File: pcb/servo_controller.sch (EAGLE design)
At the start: 54 parts, among them IC1 PIC18F452, IC2 LM2936MP-3.0, Q1 10Mhz, U1 ARDUINOR3-DIMENSION

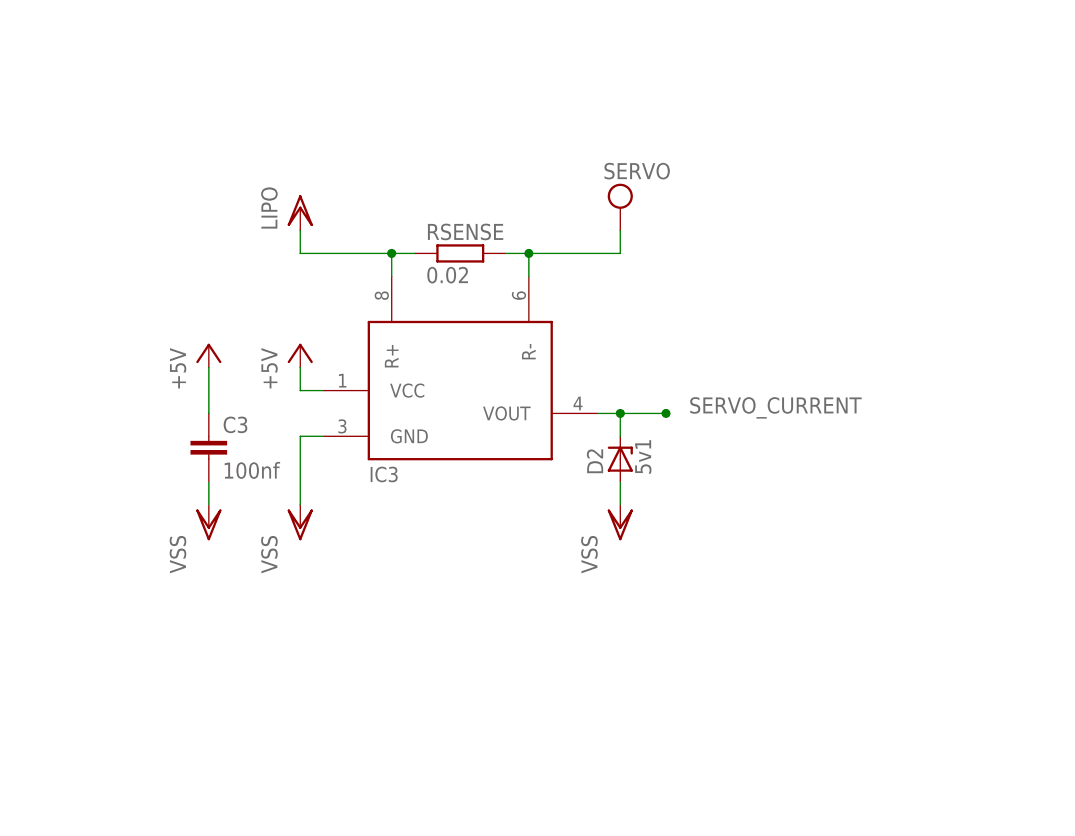
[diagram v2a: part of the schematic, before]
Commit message: Added sot23 footprint for max4173
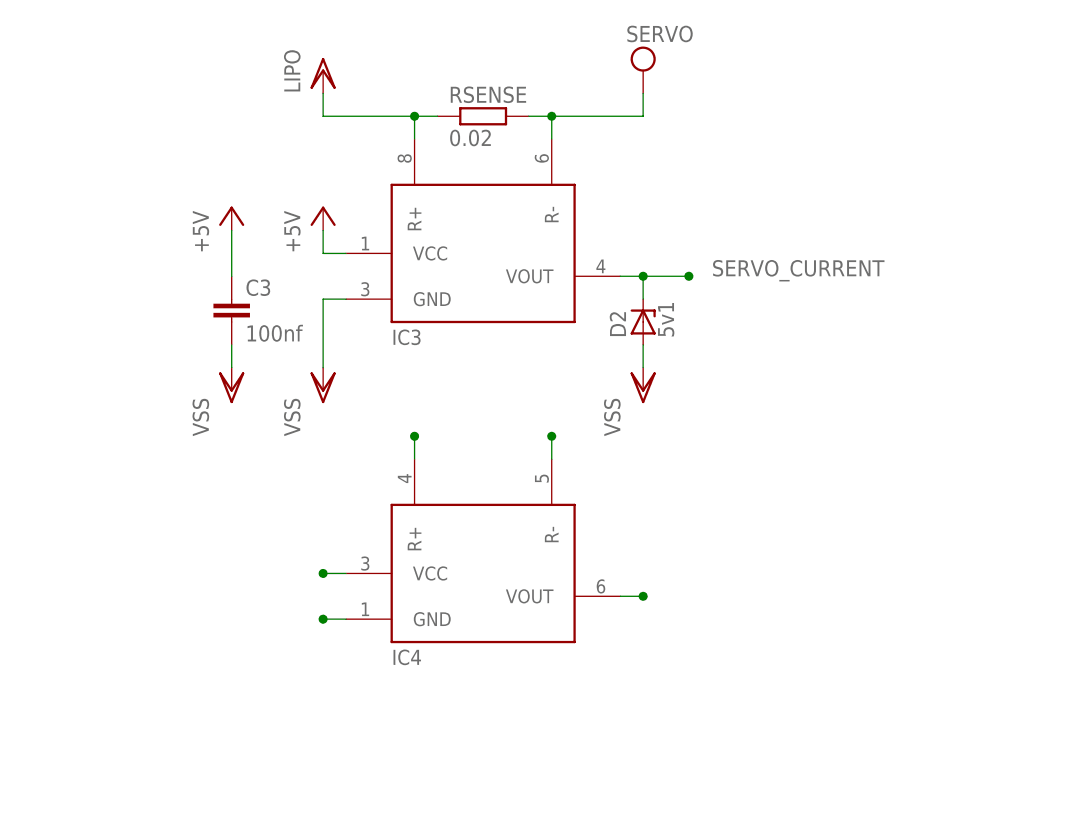
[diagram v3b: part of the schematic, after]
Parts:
- added IC4: (no value), AWJLEagleLib:MAX4173T
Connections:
- net +5V: now also IC4.VCC
- net SERVO_CURRENT: now also IC4.VOUT
- net VDD: now also IC4.R+
- net VEE: now also IC4.R-
- net VSS: now also IC4.GND
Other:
- moved on the sheet: C3, D2, IC3, RSENSE
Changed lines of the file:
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@@
 <part name="VSS27" library="supply1" deviceset="VSS" device=""/>
 <part name="PW" library="switch" deviceset="TL36PO" device=""/>
+<part name="IC4" library="AWJLEagleLib" deviceset="MAX4173" device="T"/>
 </parts>
 <sheets>
@@
 <instance part="VSS6" gate="G$1" x="48.26" y="177.8"/>
 <instance part="P+1" gate="1" x="121.92" y="215.9"/>
-<instance part="P+8" gate="1" x="193.04" y="200.66"/>
+<instance part="P+8" gate="1" x="195.58" y="215.9"/>
 <instance part="VSS7" gate="G$1" x="109.22" y="177.8"/>
 <instance part="VDD1" gate="G$1" x="48.26" y="215.9"/>
@@
 <instance part="SUPPLY3" gate="G$1" x="81.28" y="30.48"/>
 <instance part="SUPPLY4" gate="G$1" x="147.32" y="40.64"/>
-<instance part="IC3" gate="G$1" x="210.82" y="195.58"/>
-<instance part="VSS14" gate="G$1" x="193.04" y="180.34"/>
-<instance part="VDD2" gate="G$1" x="193.04" y="215.9"/>
+<instance part="IC3" gate="G$1" x="213.36" y="210.82"/>
+<instance part="VSS14" gate="G$1" x="195.58" y="195.58"/>
+<instance part="VDD2" gate="G$1" x="195.58" y="231.14"/>
 <instance part="RESET" gate="G$1" x="114.3" y="129.54" smashed="yes">
 <attribute name="NAME" x="114.935" y="130.81" size="1.778" layer="95" rot="R90"/>
@@
 <attribute name="TP_SIGNAL_NAME" x="125.73" y="128.27" size="1.778" layer="97"/>
 </instance>
-<instance part="SUPPLY5" gate="G$1" x="228.6" y="215.9"/>
+<instance part="SUPPLY5" gate="G$1" x="231.14" y="231.14"/>
 <instance part="VSS16" gate="G$1" x="134.62" y="101.6"/>
 <instance part="VSS17" gate="G$1" x="53.34" y="20.32"/>
@@
 </instance>
 <instance part="D1" gate="G$1" x="114.3" y="210.82"/>
-<instance part="C3" gate="G$1" x="182.88" y="190.5"/>
-<instance part="P+6" gate="1" x="182.88" y="200.66"/>
-<instance part="VSS8" gate="G$1" x="182.88" y="180.34"/>
+<instance part="C3" gate="G$1" x="185.42" y="205.74"/>
+<instance part="P+6" gate="1" x="185.42" y="215.9"/>
+<instance part="VSS8" gate="G$1" x="185.42" y="195.58"/>
 <instance part="EXT" gate="1" x="299.72" y="50.8"/>
 <instance part="C5" gate="G$1" x="60.96" y="30.48"/>
 <instance part="VSS22" gate="G$1" x="60.96" y="20.32"/>
-<instance part="RSENSE" gate="G$1" x="210.82" y="210.82"/>
+<instance part="RSENSE" gate="G$1" x="213.36" y="226.06"/>
 <instance part="C4" gate="G$1" x="182.88" y="27.94"/>
 <instance part="VSS23" gate="G$1" x="182.88" y="17.78"/>
@@
 <instance part="R7" gate="G$1" x="83.82" y="93.98" rot="R90"/>
 <instance part="P+9" gate="1" x="83.82" y="104.14"/>
-<instance part="D2" gate="G$1" x="228.6" y="187.96" rot="R90"/>
+<instance part="D2" gate="G$1" x="231.14" y="203.2" rot="R90"/>
 <instance part="D3" gate="G$1" x="55.88" y="187.96" rot="R90"/>
 <instance part="VSS25" gate="G$1" x="55.88" y="177.8"/>
-<instance part="VSS26" gate="G$1" x="228.6" y="180.34"/>
+<instance part="VSS26" gate="G$1" x="231.14" y="195.58"/>
 <instance part="SJ1" gate="1" x="332.74" y="129.54" rot="R90"/>
 <instance part="C9" gate="G$1" x="119.38" y="198.12"/>
 <instance part="VSS27" gate="G$1" x="119.38" y="177.8"/>
 <instance part="PW" gate="BEF1" x="35.56" y="208.28" rot="R270"/>
+<instance part="IC4" gate="G$1" x="213.36" y="175.26"/>
 </instances>
 <busses>
@@
 <segment>
 <pinref part="IC3" gate="G$1" pin="GND"/>
-<wire x1="195.58" y1="190.5" x2="193.04" y2="190.5" width="0.1524" layer="91"/>
+<wire x1="198.12" y1="205.74" x2="195.58" y2="205.74" width="0.1524" layer="91"/>
 <pinref part="VSS14" gate="G$1" pin="VSS"/>
-<wire x1="193.04" y1="190.5" x2="193.04" y2="182.88" width="0.1524" layer="91"/>
+<wire x1="195.58" y1="205.74" x2="195.58" y2="198.12" width="0.1524" layer="91"/>
 </segment>
 <segment>
@@
 <pinref part="C3" gate="G$1" pin="2"/>
 <pinref part="VSS8" gate="G$1" pin="VSS"/>
-<wire x1="182.88" y1="182.88" x2="182.88" y2="185.42" width="0.1524" layer="91"/>
+<wire x1="185.42" y1="198.12" x2="185.42" y2="200.66" width="0.1524" layer="91"/>
 </segment>
 <segment>
@@
 <pinref part="D2" gate="G$1" pin="A"/>
 <pinref part="VSS26" gate="G$1" pin="VSS"/>
-<wire x1="228.6" y1="182.88" x2="228.6" y2="185.42" width="0.1524" layer="91"/>
+<wire x1="231.14" y1="198.12" x2="231.14" y2="200.66" width="0.1524" layer="91"/>
 </segment>
 <segment>
@@
 <pinref part="VSS27" gate="G$1" pin="VSS"/>
 <wire x1="119.38" y1="180.34" x2="119.38" y2="193.04" width="0.1524" layer="91"/>
+</segment>
+<segment>
+<pinref part="IC4" gate="G$1" pin="GND"/>
+<wire x1="198.12" y1="170.18" x2="195.58" y2="170.18" width="0.1524" layer="91"/>
+<junction x="195.58" y="170.18"/>
 </segment>
 </net>
@@
 <segment>
 <pinref part="IC3" gate="G$1" pin="VCC"/>
-<wire x1="195.58" y1="195.58" x2="193.04" y2="195.58" width="0.1524" layer="91"/>
+<wire x1="198.12" y1="210.82" x2="195.58" y2="210.82" width="0.1524" layer="91"/>
 <pinref part="P+8" gate="1" pin="+5V"/>
-<wire x1="193.04" y1="195.58" x2="193.04" y2="198.12" width="0.1524" layer="91"/>
+<wire x1="195.58" y1="210.82" x2="195.58" y2="213.36" width="0.1524" layer="91"/>
 </segment>
 <segment>
 <pinref part="P+6" gate="1" pin="+5V"/>
 <pinref part="C3" gate="G$1" pin="1"/>
-<wire x1="182.88" y1="193.04" x2="182.88" y2="198.12" width="0.1524" layer="91"/>
+<wire x1="185.42" y1="208.28" x2="185.42" y2="213.36" width="0.1524" layer="91"/>
 </segment>
 <segment>
@@
 <pinref part="P+9" gate="1" pin="+5V"/>
 <wire x1="83.82" y1="101.6" x2="83.82" y2="99.06" width="0.1524" layer="91"/>
+</segment>
+<segment>
+<pinref part="IC4" gate="G$1" pin="VCC"/>
+<wire x1="198.12" y1="175.26" x2="195.58" y2="175.26" width="0.1524" layer="91"/>
+<junction x="195.58" y="175.26"/>
 </segment>
 </net>
@@
 <segment>
 <pinref part="VDD2" gate="G$1" pin="VDD"/>
-<wire x1="193.04" y1="213.36" x2="193.04" y2="210.82" width="0.1524" layer="91"/>
-<wire x1="193.04" y1="210.82" x2="203.2" y2="210.82" width="0.1524" layer="91"/>
+<wire x1="195.58" y1="228.6" x2="195.58" y2="226.06" width="0.1524" layer="91"/>
+<wire x1="195.58" y1="226.06" x2="205.74" y2="226.06" width="0.1524" layer="91"/>
 <pinref part="IC3" gate="G$1" pin="R+"/>
-<wire x1="203.2" y1="210.82" x2="203.2" y2="208.28" width="0.1524" layer="91"/>
-<wire x1="203.2" y1="210.82" x2="205.74" y2="210.82" width="0.1524" layer="91"/>
-<junction x="203.2" y="210.82"/>
+<wire x1="205.74" y1="226.06" x2="205.74" y2="223.52" width="0.1524" layer="91"/>
+<wire x1="205.74" y1="226.06" x2="208.28" y2="226.06" width="0.1524" layer="91"/>
+<junction x="205.74" y="226.06"/>
 <pinref part="RSENSE" gate="G$1" pin="1"/>
+</segment>
+<segment>
+<pinref part="IC4" gate="G$1" pin="R+"/>
+<wire x1="205.74" y1="187.96" x2="205.74" y2="190.5" width="0.1524" layer="91"/>
+<junction x="205.74" y="190.5"/>
 </segment>
 </net>
@@
 <segment>
 <pinref part="IC3" gate="G$1" pin="R-"/>
-<wire x1="218.44" y1="208.28" x2="218.44" y2="210.82" width="0.1524" layer="91"/>
-<wire x1="218.44" y1="210.82" x2="228.6" y2="210.82" width="0.1524" layer="91"/>
+<wire x1="220.98" y1="223.52" x2="220.98" y2="226.06" width="0.1524" layer="91"/>
+<wire x1="220.98" y1="226.06" x2="231.14" y2="226.06" width="0.1524" layer="91"/>
 <pinref part="SUPPLY5" gate="G$1" pin="VEE"/>
-<wire x1="228.6" y1="210.82" x2="228.6" y2="213.36" width="0.1524" layer="91"/>
-<wire x1="215.9" y1="210.82" x2="218.44" y2="210.82" width="0.1524" layer="91"/>
-<junction x="218.44" y="210.82"/>
+<wire x1="231.14" y1="226.06" x2="231.14" y2="228.6" width="0.1524" layer="91"/>
+<wire x1="218.44" y1="226.06" x2="220.98" y2="226.06" width="0.1524" layer="91"/>
+<junction x="220.98" y="226.06"/>
 <pinref part="RSENSE" gate="G$1" pin="2"/>
 </segment>
+<segment>
+<pinref part="IC4" gate="G$1" pin="R-"/>
+<wire x1="220.98" y1="187.96" x2="220.98" y2="190.5" width="0.1524" layer="91"/>
+<junction x="220.98" y="190.5"/>
+</segment>
 </net>
 <net name="SERVO_CURRENT" class="0">
 <segment>
 <pinref part="IC3" gate="G$1" pin="VOUT"/>
-<wire x1="226.06" y1="193.04" x2="228.6" y2="193.04" width="0.1524" layer="91"/>
-<junction x="233.68" y="193.04"/>
-<label x="236.22" y="193.04" size="1.778" layer="95"/>
+<wire x1="228.6" y1="208.28" x2="231.14" y2="208.28" width="0.1524" layer="91"/>
+<junction x="236.22" y="208.28"/>
+<label x="238.76" y="208.28" size="1.778" layer="95"/>
 <pinref part="D2" gate="G$1" pin="C"/>
-<wire x1="228.6" y1="193.04" x2="233.68" y2="193.04" width="0.1524" layer="91"/>
-<wire x1="228.6" y1="193.04" x2="228.6" y2="190.5" width="0.1524" layer="91"/>
-<junction x="228.6" y="193.04"/>
+<wire x1="231.14" y1="208.28" x2="236.22" y2="208.28" width="0.1524" layer="91"/>
+<wire x1="231.14" y1="208.28" x2="231.14" y2="205.74" width="0.1524" layer="91"/>
+<junction x="231.14" y="208.28"/>
 </segment>
 <segment>
@@
 <label x="353.06" y="116.84" size="1.778" layer="95" rot="R90"/>
 </segment>
-</net>
+<segment>
+<pinref part="IC4" gate="G$1" pin="VOUT"/>
+<wire x1="228.6" y1="172.72" x2="231.14" y2="172.72" width="0.1524" layer="91"/>
+<junction x="231.14" y="172.72"/>
+</segment>
+</net>

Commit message: Misc
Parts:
- IC3: value (none) -> MAX4173FESA+
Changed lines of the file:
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@@
 <part name="SUPPLY3" library="supply2" deviceset="VEE" device="" value="SERVO"/>
 <part name="SUPPLY4" library="supply2" deviceset="VEE" device="" value="SERVO"/>
-<part name="IC3" library="AWJLEagleLib" deviceset="MAX4173" device="A"/>
+<part name="IC3" library="AWJLEagleLib" deviceset="MAX4173" device="A" value="MAX4173FESA+"/>
 <part name="VSS14" library="supply1" deviceset="VSS" device=""/>
 <part name="VDD2" library="supply1" deviceset="VDD" device="" value="LIPO"/>

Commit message: Elec
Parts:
- removed IC4: (no value), AWJLEagleLib:MAX4173T
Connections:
- net +5V: no longer IC4.VCC
- net SERVO_CURRENT: no longer IC4.VOUT
- net VDD: no longer IC4.R+
- net VEE: no longer IC4.R-
- net VSS: no longer IC4.GND
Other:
- moved on the sheet: C3, D2, IC3, RSENSE
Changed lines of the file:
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@@
 <part name="VSS27" library="supply1" deviceset="VSS" device=""/>
 <part name="PW" library="switch" deviceset="TL36PO" device=""/>
-<part name="IC4" library="AWJLEagleLib" deviceset="MAX4173" device="T"/>
 </parts>
 <sheets>
@@
 <instance part="VSS6" gate="G$1" x="48.26" y="177.8"/>
 <instance part="P+1" gate="1" x="121.92" y="215.9"/>
-<instance part="P+8" gate="1" x="195.58" y="215.9"/>
+<instance part="P+8" gate="1" x="198.12" y="205.74"/>
 <instance part="VSS7" gate="G$1" x="109.22" y="177.8"/>
 <instance part="VDD1" gate="G$1" x="48.26" y="215.9"/>
@@
 <instance part="SUPPLY3" gate="G$1" x="81.28" y="30.48"/>
 <instance part="SUPPLY4" gate="G$1" x="147.32" y="40.64"/>
-<instance part="IC3" gate="G$1" x="213.36" y="210.82"/>
-<instance part="VSS14" gate="G$1" x="195.58" y="195.58"/>
-<instance part="VDD2" gate="G$1" x="195.58" y="231.14"/>
+<instance part="IC3" gate="G$1" x="215.9" y="200.66"/>
+<instance part="VSS14" gate="G$1" x="198.12" y="185.42"/>
+<instance part="VDD2" gate="G$1" x="198.12" y="220.98"/>
 <instance part="RESET" gate="G$1" x="114.3" y="129.54" smashed="yes">
 <attribute name="NAME" x="114.935" y="130.81" size="1.778" layer="95" rot="R90"/>
@@
 <attribute name="TP_SIGNAL_NAME" x="125.73" y="128.27" size="1.778" layer="97"/>
 </instance>
-<instance part="SUPPLY5" gate="G$1" x="231.14" y="231.14"/>
+<instance part="SUPPLY5" gate="G$1" x="233.68" y="220.98"/>
 <instance part="VSS16" gate="G$1" x="134.62" y="101.6"/>
 <instance part="VSS17" gate="G$1" x="53.34" y="20.32"/>
@@
 </instance>
 <instance part="D1" gate="G$1" x="114.3" y="210.82"/>
-<instance part="C3" gate="G$1" x="185.42" y="205.74"/>
-<instance part="P+6" gate="1" x="185.42" y="215.9"/>
-<instance part="VSS8" gate="G$1" x="185.42" y="195.58"/>
+<instance part="C3" gate="G$1" x="187.96" y="195.58"/>
+<instance part="P+6" gate="1" x="187.96" y="205.74"/>
+<instance part="VSS8" gate="G$1" x="187.96" y="185.42"/>
 <instance part="EXT" gate="1" x="299.72" y="50.8"/>
 <instance part="C5" gate="G$1" x="60.96" y="30.48"/>
 <instance part="VSS22" gate="G$1" x="60.96" y="20.32"/>
-<instance part="RSENSE" gate="G$1" x="213.36" y="226.06"/>
+<instance part="RSENSE" gate="G$1" x="215.9" y="215.9"/>
 <instance part="C4" gate="G$1" x="182.88" y="27.94"/>
 <instance part="VSS23" gate="G$1" x="182.88" y="17.78"/>
@@
 <instance part="R7" gate="G$1" x="83.82" y="93.98" rot="R90"/>
 <instance part="P+9" gate="1" x="83.82" y="104.14"/>
-<instance part="D2" gate="G$1" x="231.14" y="203.2" rot="R90"/>
+<instance part="D2" gate="G$1" x="233.68" y="193.04" rot="R90"/>
 <instance part="D3" gate="G$1" x="55.88" y="187.96" rot="R90"/>
 <instance part="VSS25" gate="G$1" x="55.88" y="177.8"/>
-<instance part="VSS26" gate="G$1" x="231.14" y="195.58"/>
+<instance part="VSS26" gate="G$1" x="233.68" y="185.42"/>
 <instance part="SJ1" gate="1" x="332.74" y="129.54" rot="R90"/>
 <instance part="C9" gate="G$1" x="119.38" y="198.12"/>
 <instance part="VSS27" gate="G$1" x="119.38" y="177.8"/>
 <instance part="PW" gate="BEF1" x="35.56" y="208.28" rot="R270"/>
-<instance part="IC4" gate="G$1" x="213.36" y="175.26"/>
 </instances>
 <busses>
@@
 <segment>
 <pinref part="IC3" gate="G$1" pin="GND"/>
-<wire x1="198.12" y1="205.74" x2="195.58" y2="205.74" width="0.1524" layer="91"/>
+<wire x1="200.66" y1="195.58" x2="198.12" y2="195.58" width="0.1524" layer="91"/>
 <pinref part="VSS14" gate="G$1" pin="VSS"/>
-<wire x1="195.58" y1="205.74" x2="195.58" y2="198.12" width="0.1524" layer="91"/>
+<wire x1="198.12" y1="195.58" x2="198.12" y2="187.96" width="0.1524" layer="91"/>
 </segment>
 <segment>
@@
 <pinref part="C3" gate="G$1" pin="2"/>
 <pinref part="VSS8" gate="G$1" pin="VSS"/>
-<wire x1="185.42" y1="198.12" x2="185.42" y2="200.66" width="0.1524" layer="91"/>
+<wire x1="187.96" y1="187.96" x2="187.96" y2="190.5" width="0.1524" layer="91"/>
 </segment>
 <segment>
@@
 <pinref part="D2" gate="G$1" pin="A"/>
 <pinref part="VSS26" gate="G$1" pin="VSS"/>
-<wire x1="231.14" y1="198.12" x2="231.14" y2="200.66" width="0.1524" layer="91"/>
+<wire x1="233.68" y1="187.96" x2="233.68" y2="190.5" width="0.1524" layer="91"/>
 </segment>
 <segment>
@@
 <pinref part="VSS27" gate="G$1" pin="VSS"/>
 <wire x1="119.38" y1="180.34" x2="119.38" y2="193.04" width="0.1524" layer="91"/>
-</segment>
-<segment>
-<pinref part="IC4" gate="G$1" pin="GND"/>
-<wire x1="198.12" y1="170.18" x2="195.58" y2="170.18" width="0.1524" layer="91"/>
-<junction x="195.58" y="170.18"/>
 </segment>
 </net>
@@
 <segment>
 <pinref part="IC3" gate="G$1" pin="VCC"/>
-<wire x1="198.12" y1="210.82" x2="195.58" y2="210.82" width="0.1524" layer="91"/>
+<wire x1="200.66" y1="200.66" x2="198.12" y2="200.66" width="0.1524" layer="91"/>
 <pinref part="P+8" gate="1" pin="+5V"/>
-<wire x1="195.58" y1="210.82" x2="195.58" y2="213.36" width="0.1524" layer="91"/>
+<wire x1="198.12" y1="200.66" x2="198.12" y2="203.2" width="0.1524" layer="91"/>
 </segment>
 <segment>
 <pinref part="P+6" gate="1" pin="+5V"/>
 <pinref part="C3" gate="G$1" pin="1"/>
-<wire x1="185.42" y1="208.28" x2="185.42" y2="213.36" width="0.1524" layer="91"/>
+<wire x1="187.96" y1="198.12" x2="187.96" y2="203.2" width="0.1524" layer="91"/>
 </segment>
 <segment>
@@
 <pinref part="P+9" gate="1" pin="+5V"/>
 <wire x1="83.82" y1="101.6" x2="83.82" y2="99.06" width="0.1524" layer="91"/>
-</segment>
-<segment>
-<pinref part="IC4" gate="G$1" pin="VCC"/>
-<wire x1="198.12" y1="175.26" x2="195.58" y2="175.26" width="0.1524" layer="91"/>
-<junction x="195.58" y="175.26"/>
 </segment>
 </net>
@@
 <segment>
 <pinref part="VDD2" gate="G$1" pin="VDD"/>
-<wire x1="195.58" y1="228.6" x2="195.58" y2="226.06" width="0.1524" layer="91"/>
-<wire x1="195.58" y1="226.06" x2="205.74" y2="226.06" width="0.1524" layer="91"/>
+<wire x1="198.12" y1="218.44" x2="198.12" y2="215.9" width="0.1524" layer="91"/>
+<wire x1="198.12" y1="215.9" x2="208.28" y2="215.9" width="0.1524" layer="91"/>
 <pinref part="IC3" gate="G$1" pin="R+"/>
-<wire x1="205.74" y1="226.06" x2="205.74" y2="223.52" width="0.1524" layer="91"/>
-<wire x1="205.74" y1="226.06" x2="208.28" y2="226.06" width="0.1524" layer="91"/>
-<junction x="205.74" y="226.06"/>
+<wire x1="208.28" y1="215.9" x2="208.28" y2="213.36" width="0.1524" layer="91"/>
+<wire x1="208.28" y1="215.9" x2="210.82" y2="215.9" width="0.1524" layer="91"/>
+<junction x="208.28" y="215.9"/>
 <pinref part="RSENSE" gate="G$1" pin="1"/>
-</segment>
-<segment>
-<pinref part="IC4" gate="G$1" pin="R+"/>
-<wire x1="205.74" y1="187.96" x2="205.74" y2="190.5" width="0.1524" layer="91"/>
-<junction x="205.74" y="190.5"/>
 </segment>
 </net>
@@
 <segment>
 <pinref part="IC3" gate="G$1" pin="R-"/>
-<wire x1="220.98" y1="223.52" x2="220.98" y2="226.06" width="0.1524" layer="91"/>
-<wire x1="220.98" y1="226.06" x2="231.14" y2="226.06" width="0.1524" layer="91"/>
+<wire x1="223.52" y1="213.36" x2="223.52" y2="215.9" width="0.1524" layer="91"/>
+<wire x1="223.52" y1="215.9" x2="233.68" y2="215.9" width="0.1524" layer="91"/>
 <pinref part="SUPPLY5" gate="G$1" pin="VEE"/>
-<wire x1="231.14" y1="226.06" x2="231.14" y2="228.6" width="0.1524" layer="91"/>
-<wire x1="218.44" y1="226.06" x2="220.98" y2="226.06" width="0.1524" layer="91"/>
-<junction x="220.98" y="226.06"/>
+<wire x1="233.68" y1="215.9" x2="233.68" y2="218.44" width="0.1524" layer="91"/>
+<wire x1="220.98" y1="215.9" x2="223.52" y2="215.9" width="0.1524" layer="91"/>
+<junction x="223.52" y="215.9"/>
 <pinref part="RSENSE" gate="G$1" pin="2"/>
 </segment>
-<segment>
-<pinref part="IC4" gate="G$1" pin="R-"/>
-<wire x1="220.98" y1="187.96" x2="220.98" y2="190.5" width="0.1524" layer="91"/>
-<junction x="220.98" y="190.5"/>
-</segment>
 </net>
 <net name="SERVO_CURRENT" class="0">
 <segment>
 <pinref part="IC3" gate="G$1" pin="VOUT"/>
-<wire x1="228.6" y1="208.28" x2="231.14" y2="208.28" width="0.1524" layer="91"/>
-<junction x="236.22" y="208.28"/>
-<label x="238.76" y="208.28" size="1.778" layer="95"/>
+<wire x1="231.14" y1="198.12" x2="233.68" y2="198.12" width="0.1524" layer="91"/>
+<junction x="238.76" y="198.12"/>
+<label x="241.3" y="198.12" size="1.778" layer="95"/>
 <pinref part="D2" gate="G$1" pin="C"/>
-<wire x1="231.14" y1="208.28" x2="236.22" y2="208.28" width="0.1524" layer="91"/>
-<wire x1="231.14" y1="208.28" x2="231.14" y2="205.74" width="0.1524" layer="91"/>
-<junction x="231.14" y="208.28"/>
+<wire x1="233.68" y1="198.12" x2="238.76" y2="198.12" width="0.1524" layer="91"/>
+<wire x1="233.68" y1="198.12" x2="233.68" y2="195.58" width="0.1524" layer="91"/>
+<junction x="233.68" y="198.12"/>
 </segment>
 <segment>
@@
 <label x="353.06" y="116.84" size="1.778" layer="95" rot="R90"/>
 </segment>
-<segment>
-<pinref part="IC4" gate="G$1" pin="VOUT"/>
-<wire x1="228.6" y1="172.72" x2="231.14" y2="172.72" width="0.1524" layer="91"/>
-<junction x="231.14" y="172.72"/>
-</segment>
-</net>
+</net>
